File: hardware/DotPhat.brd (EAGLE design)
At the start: 30 x 65 mm, 56 parts, among them CN1 1X4-BIG, IC1 CAT24M010TS, IC3 SI1145, J3 USB-MICROB, Q1 BSH103, U1 ATMEGA328P-MU-QFN32, U2 TMP102, U3 ATSHA204-TSU, X2 MC-RTC-RV-4162-C7-I2C, X3 S4B-ZR

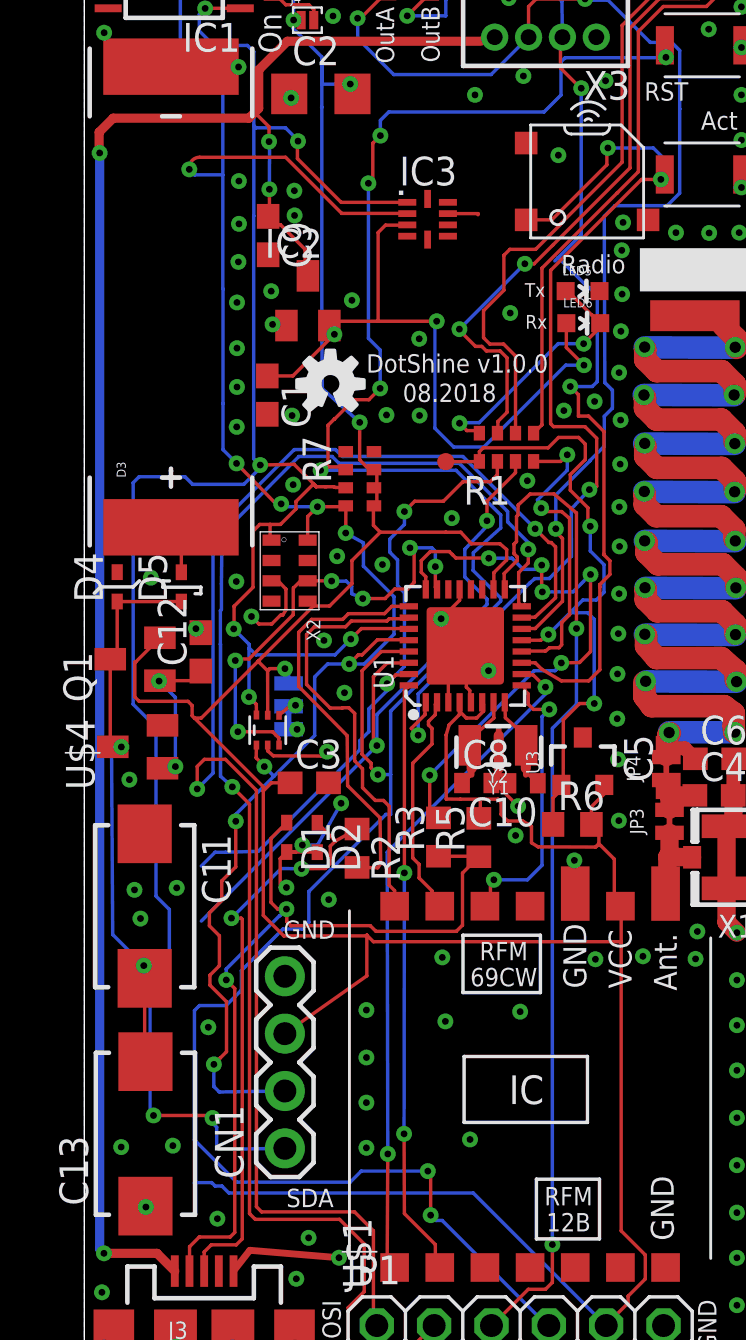
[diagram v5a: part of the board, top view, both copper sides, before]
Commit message: Add SJ for bypass threshold VCC, polarity markers
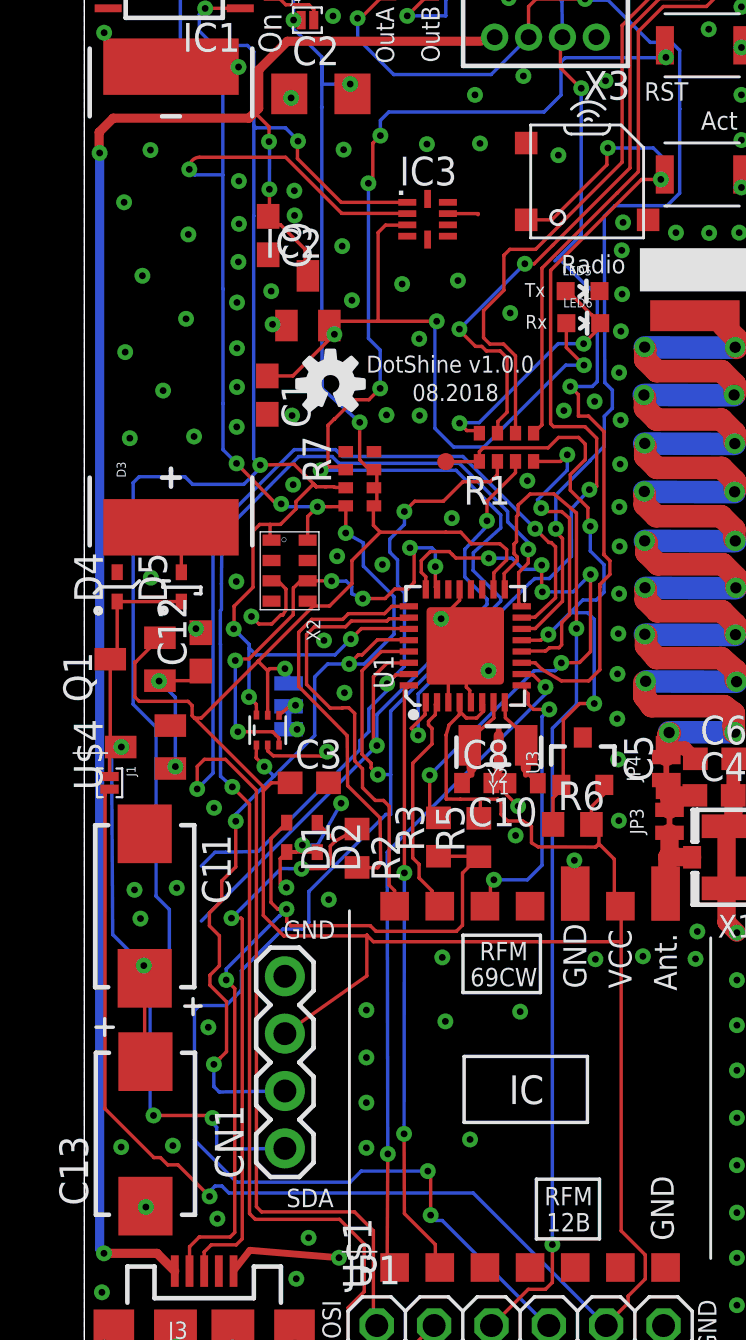
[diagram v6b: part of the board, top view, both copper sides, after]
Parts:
- added J1: (no value), solderjumper:2.MED
- moved U$4 0.35 mm to (2.71, 27.5)
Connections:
- net +3V3: now also J1.2
- net CAPS_VCC: now also J1.1
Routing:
- net +3V3: track 214.0 -> 234.3 mm, vias 8 -> 9
- net CAPS_VCC: track 24.9 -> 27.2 mm
- net GND: vias 130 -> 145
